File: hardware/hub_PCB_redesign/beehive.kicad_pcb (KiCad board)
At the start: 2 copper layers, 76 x 85 mm, 36 parts, among them CON1 BARREL_JACK, J1 USB_A, P1 D1, P10 A2, P11 A3, P12 UART, P13 I2C 1, P14 I2C 2, P15 12V, P2 D2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

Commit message: update main hub
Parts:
- removed the   at (139.5, 70.5)
- U1, U2: value LM2596 -> LM2596T-5
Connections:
- P1 pad 1: +5V -> D1-3
- P1 pad 2: GND -> D1-4
- P1 pad 3: D1-3 -> +5V
- P1 pad 4: D1-4 -> GND
- P10 pad 1: +5V -> A2-3
- P10 pad 2: GND -> A2-4
- P10 pad 3: A2-3 -> +5V
- P10 pad 4: A2-4 -> GND
- P11 pad 1: +5V -> A3-3
- P11 pad 2: GND -> A3-4
- P11 pad 3: A3-3 -> +5V
- P11 pad 4: A3-4 -> GND
- P12 pad 1: +5V -> TX
- P12 pad 2: GND -> RX
- P12 pad 3: TX -> +5V
- P12 pad 4: RX -> GND
- P13 pad 1: +5V -> I2C_1-3
- P13 pad 2: GND -> I2C_1-4
- P13 pad 3: I2C_1-3 -> +5V
- P13 pad 4: I2C_1-4 -> GND
- P14 pad 1: +5V -> I2C_2-3
- P14 pad 2: GND -> I2C_2-4
- P14 pad 3: I2C_2-3 -> +5V
- P14 pad 4: I2C_2-4 -> GND
- P15 pad 1: Net-(C1-Pad1) -> Net-(P15-Pad1)
- P15 pad 2: GND -> Net-(P15-Pad2)
- P15 pad 3: Net-(P15-Pad3) -> Net-(C1-Pad1)
- P15 pad 4: Net-(P15-Pad4) -> GND
- P2 pad 1: +5V -> D2-3
- P2 pad 2: GND -> D2-4
- P2 pad 3: D2-3 -> +5V
- P2 pad 4: D2-4 -> GND
- P3 pad 1: +5V -> D3-3
- P3 pad 2: GND -> D3-4
- P3 pad 3: D3-3 -> +5V
- P3 pad 4: D3-4 -> GND
- P4 pad 1: +5V -> D4-3
- P4 pad 2: GND -> D4-4
- P4 pad 3: D4-3 -> +5V
- P4 pad 4: D4-4 -> GND
- P5 pad 1: +5V -> D5-3
- P5 pad 2: GND -> D5-4
- P5 pad 3: D5-3 -> +5V
- P5 pad 4: D5-4 -> GND
- P6 pad 1: +5V -> D6-3
- P6 pad 2: GND -> D6-4
- P6 pad 3: D6-3 -> +5V
- P6 pad 4: D6-4 -> GND
- P7 pad 1: +5V -> D7-3
- P7 pad 2: GND -> D7-4
- P7 pad 3: D7-3 -> +5V
- P7 pad 4: D7-4 -> GND
- P8 pad 1: +5V -> D8-3
- P8 pad 2: GND -> D8-4
- P8 pad 3: D8-3 -> +5V
- P8 pad 4: D8-4 -> GND
- P9 pad 1: +5V -> A1-3
- P9 pad 2: GND -> A1-4
- P9 pad 3: A1-3 -> +5V
- P9 pad 4: A1-4 -> GND
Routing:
- net GND: track 18.6 -> 7.07 mm
- net A2-4: track 32.7 -> 27.4 mm
- net A2-3: track 32.4 -> 27.4 mm
- net I2C_2-4: track 80.3 -> 85.3 mm
- net I2C_2-3: track 75.0 -> 80.0 mm
- net A3-4: track 43.8 -> 38.8 mm
- net A3-3: track 38.0 -> 33.0 mm
- net A1-4: track 41.2 -> 36.2 mm
- net A1-3: track 41.2 -> 36.2 mm
- net D4-3: track 14.0 -> 10.0 mm
- net D4-4: track 14.0 -> 10.0 mm
- net D6-4: track 12.3 -> 9.07 mm
- net Net-(C1-Pad1): track 86.5 -> 89.5 mm
- net D5-4: track 26.5 -> 23.8 mm
- net D8-4: track 55.8 -> 53.1 mm
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
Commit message: update central hub silk --> channel names
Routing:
- net GND: track 7.07 -> 0.00 mm

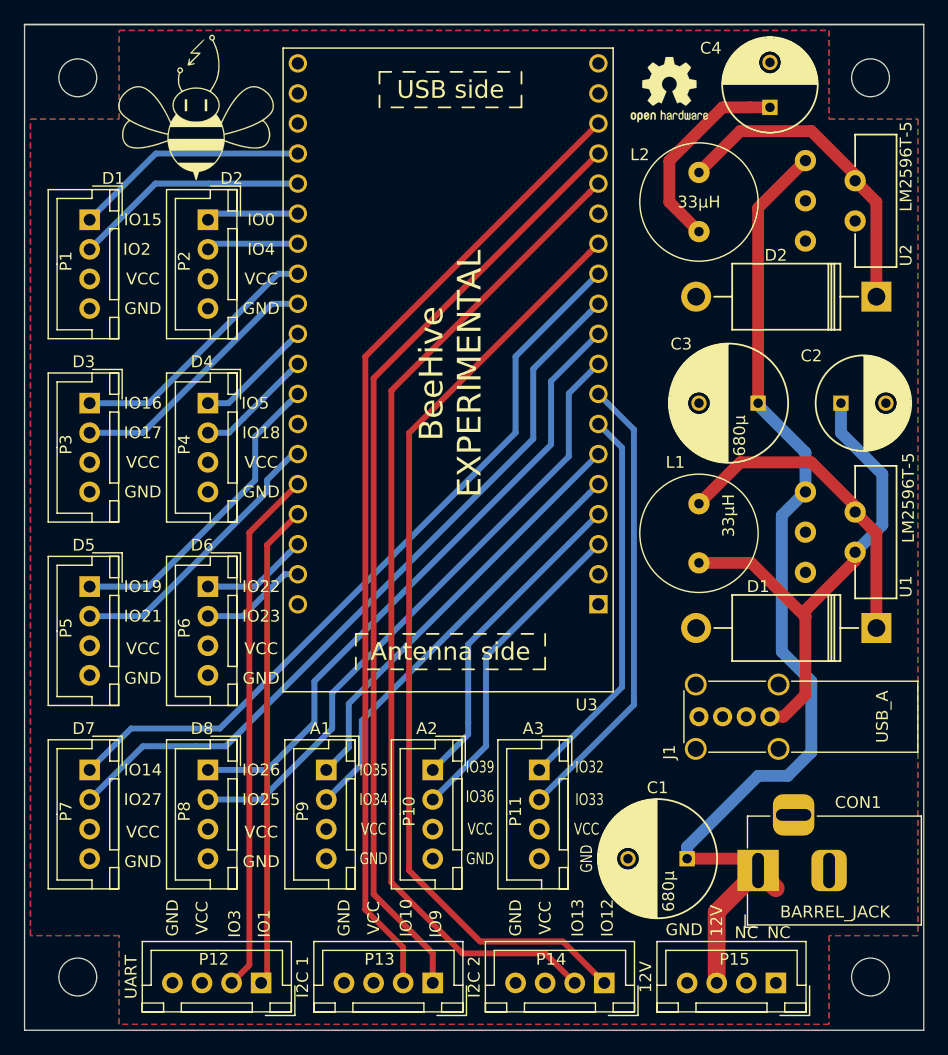
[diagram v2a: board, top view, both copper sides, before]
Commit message: Update on 12V5A system power line
- 12V5A power line is now represented by two connectors with 2 pins across all the modules
- all .png previews are updated. The central hub now has previews for schematics, PCB tracing and 3D model
- peltier module now has two 12V5A connectors with redesigned one side of the bridge. Now all MOSFETs can be equipped with heatsinks
- hum/temp sensor now has its connector position reversed to mimic Grove's one
- hum/temp and gas sensors now have a small BeeHive logo on front layer rather than one big on back layer
- hum/temp sensor now use only one layer for signals and one layer for ground
- switch arrays now have two connectors for 12V5A and 5V3A power lines
- switch arrays had their power lines better traced (no sharp turns)
- power supply (12V5A to 5V3A) now has two connectors for 12V5A power line
- one trace of power supply, which lies in between LM2596's legs, was narrowed to ensure that it will not be accidentally soldered or damaged during placement
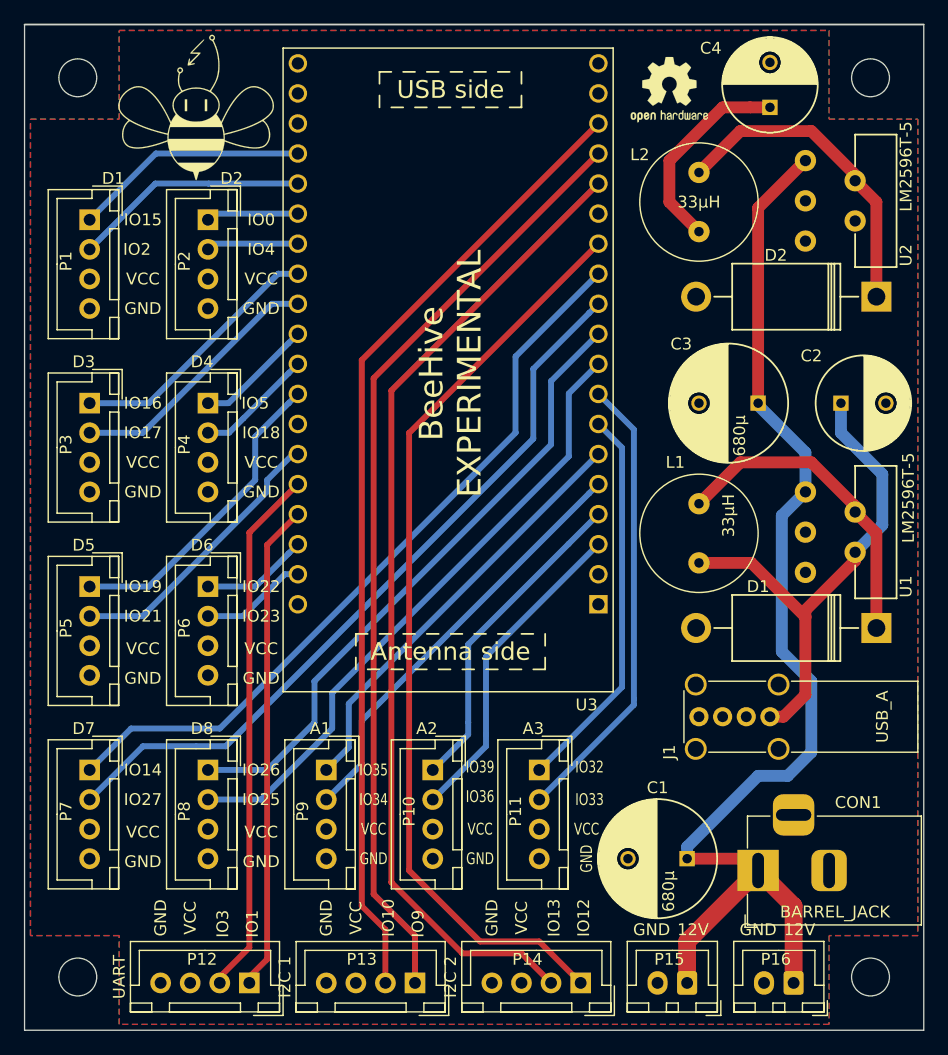
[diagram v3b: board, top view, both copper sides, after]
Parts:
- added P16: Conn_01x02, Connector_JST:JST_XH_B2B-XH-A_1x02_P2.50mm_Vertical, F.Cu at (191.0, 141.0)
- P15: value 12V -> Conn_01x02; footprint Connector_JST:JST_XH_B04B-XH-A_04x2.50mm_Straight -> Connector_JST:JST_XH_B2B-XH-A_1x02_P2.50mm_Vertical
- moved P14 2.00 mm to (182.0, 141.0)
- moved P13 1.50 mm to (168.0, 141.0)
- moved P15 1.50 mm to (200.0, 141.0)
- moved P12 1.00 mm to (154.0, 141.0)
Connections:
- P15 pad 1: Net-(P15-Pad1) -> Net-(C1-Pad1)
- P15 pad 2: Net-(P15-Pad2) -> GND
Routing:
- net Net-(C1-Pad1): track 89.5 -> 99.1 mm
- net I2C_2-4: track 85.3 -> 83.3 mm
- net I2C_2-3: track 80.0 -> 78.0 mm
- net I2C_1-3: track 80.0 -> 79.4 mm
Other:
- board text removed: "NC"

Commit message: Add version number to boards
Add version number to boards and update screenshots, zip gerber archives
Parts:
- removed the G*** at (149.5, 67.0)
- added G***: LOGO, logo-beehive:logo-beehive-7_2х6_7mm, F.Cu at (148.5, 64.0)
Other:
- board text added: "BeeHive v0.3"
- board text removed: "BeeHive EXPERIMENTAL"

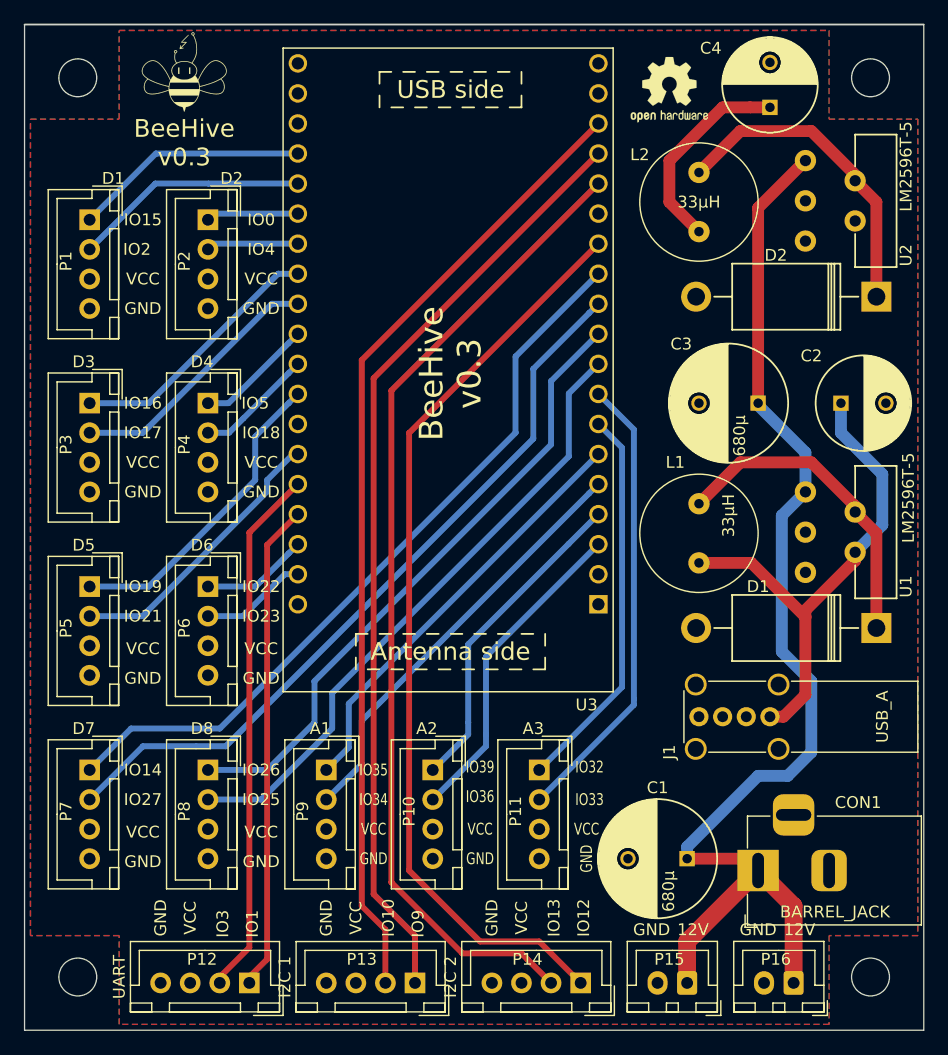
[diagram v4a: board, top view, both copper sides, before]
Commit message: Add ESP32 5V trace and minor changes
ESP32 is now connected to the same line as Raspberry Pi that should reduce the noise.
Add new screenshot to the temperature breakout board

Co-Authored-By: Andre Maia Chagas <a.maia-chagas@sussex.ac.uk>
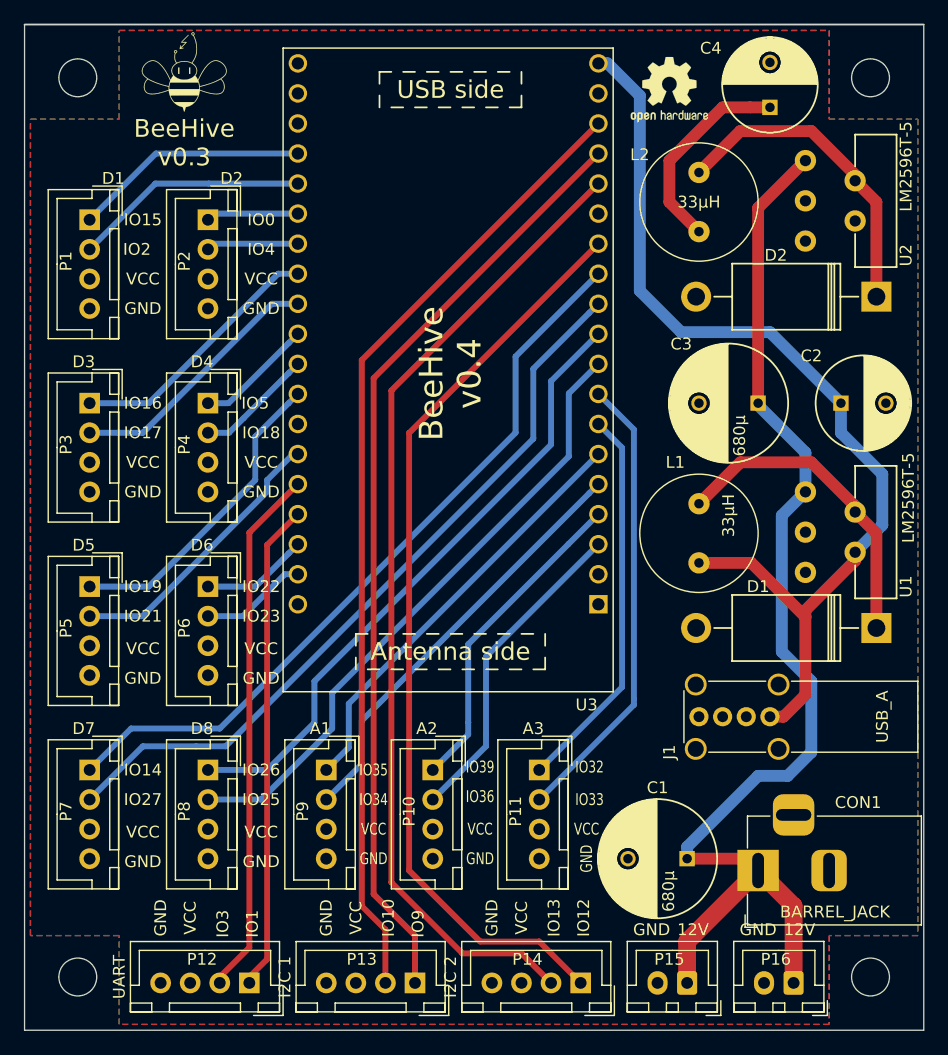
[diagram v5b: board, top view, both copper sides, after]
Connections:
- C2 pad 1: Net-(C2-Pad1) -> ESP_pow
- J1 pad 1: Net-(C2-Pad1) -> ESP_pow
- L1 pad 2: Net-(C2-Pad1) -> ESP_pow
- U1 pad 4: Net-(C2-Pad1) -> ESP_pow
- U3 pad 19: +5V -> ESP_pow
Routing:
- net ESP_pow: track 0.00 -> 85.5 mm
- net Net-(C2-Pad1): track 43.4 -> 0.00 mm
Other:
- board text added: "BeeHive v0.4"

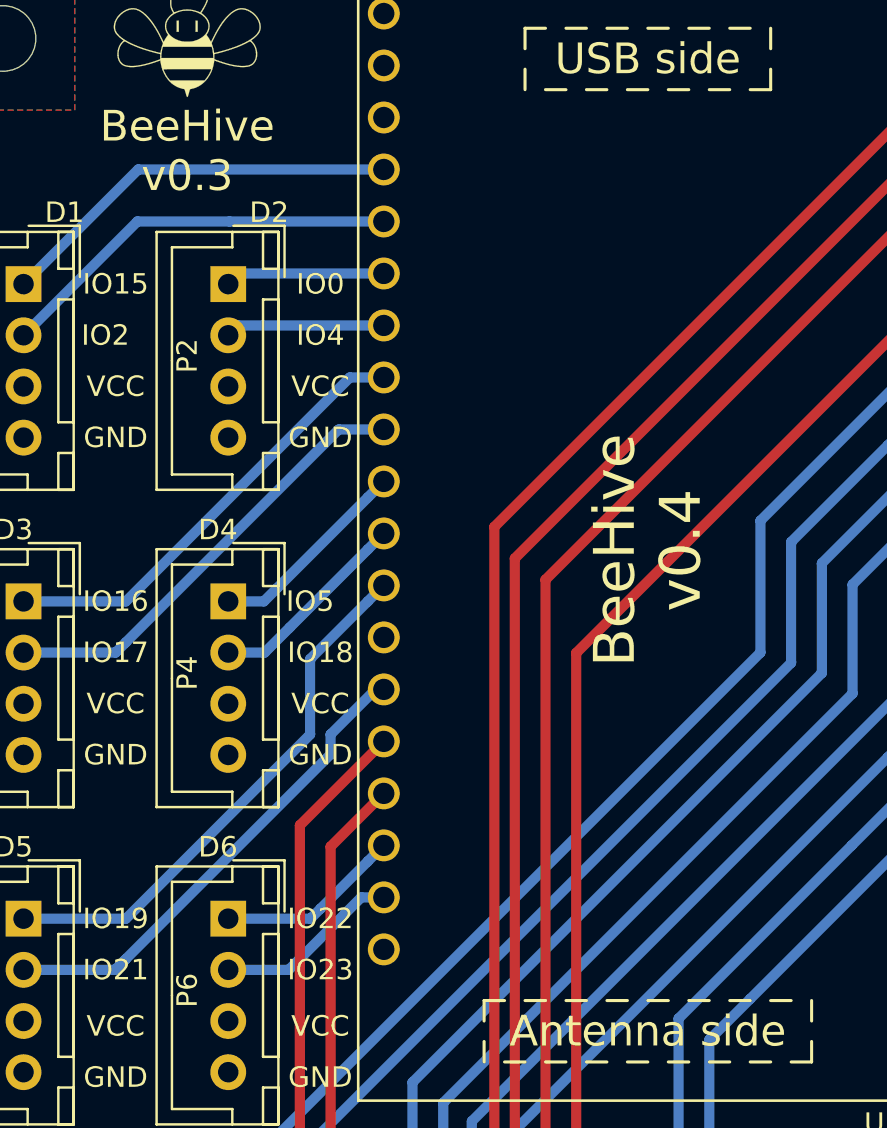
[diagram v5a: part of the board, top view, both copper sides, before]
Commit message: Apply CERN-W license
Apply CERN-W license to all boards, move the first iteration of the IR_sensor to the archive

Co-Authored-By: Andre Maia Chagas <a.maia-chagas@sussex.ac.uk>
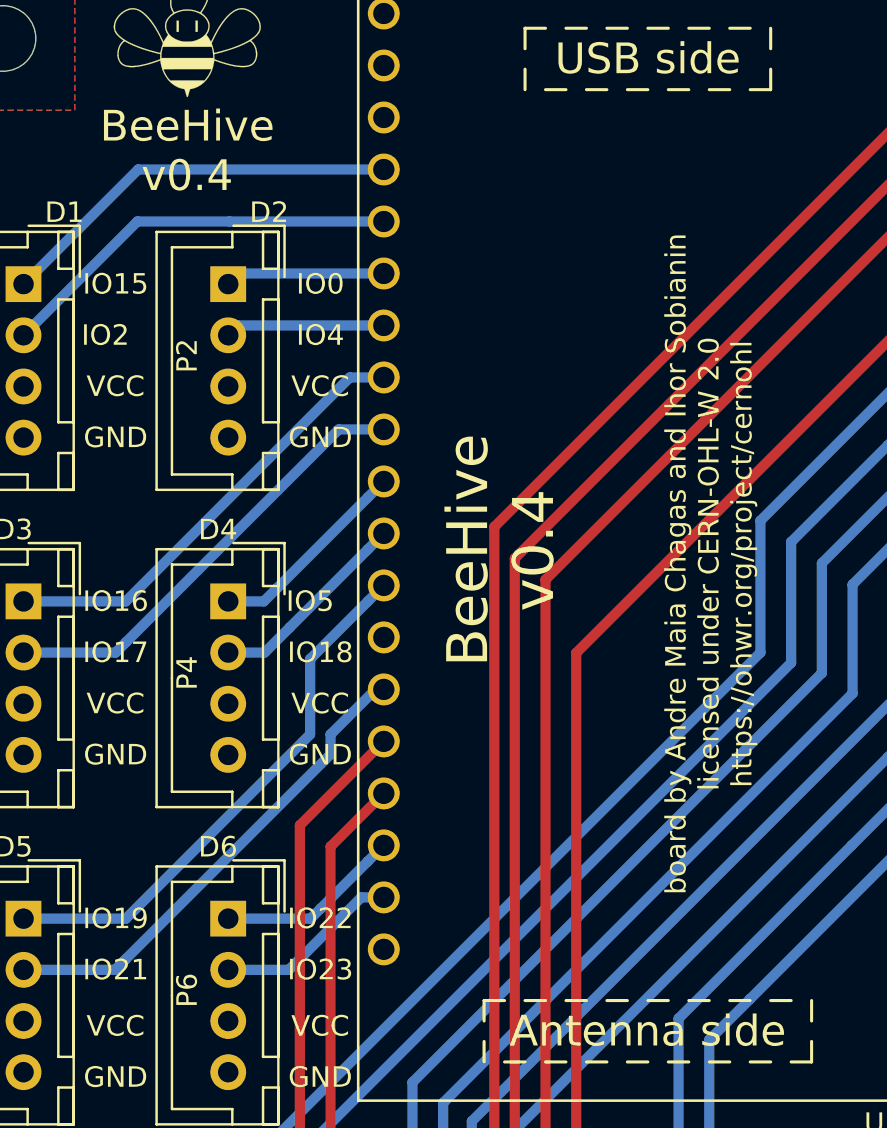
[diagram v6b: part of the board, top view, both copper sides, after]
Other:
- board text added: "board by Andre Maia Chagas and Ihor Sobianin licensed under CERN-OHL-W 2.0 https://ohwr.org/project/cernohl"
- board text removed: "BeeHive v0.3"
